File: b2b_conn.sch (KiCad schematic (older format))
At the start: 3 parts

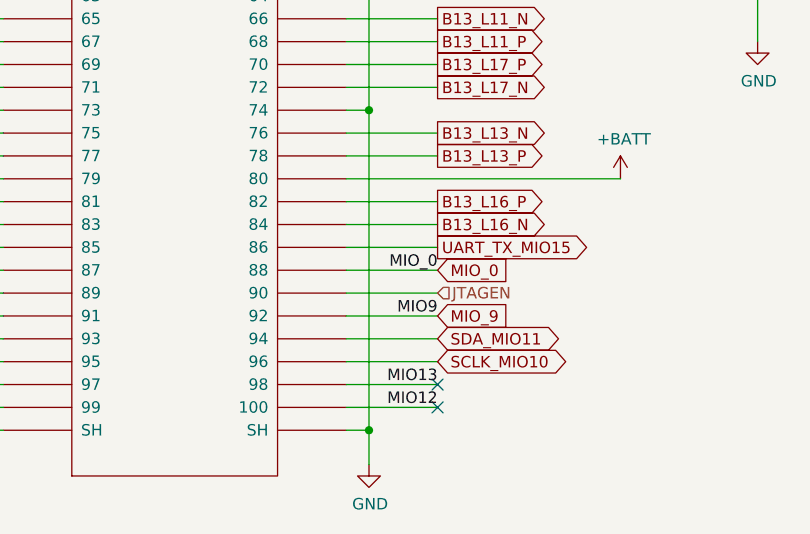
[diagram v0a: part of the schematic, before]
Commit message: b2b_conn.sch: removed redundant local labels (globals already present)
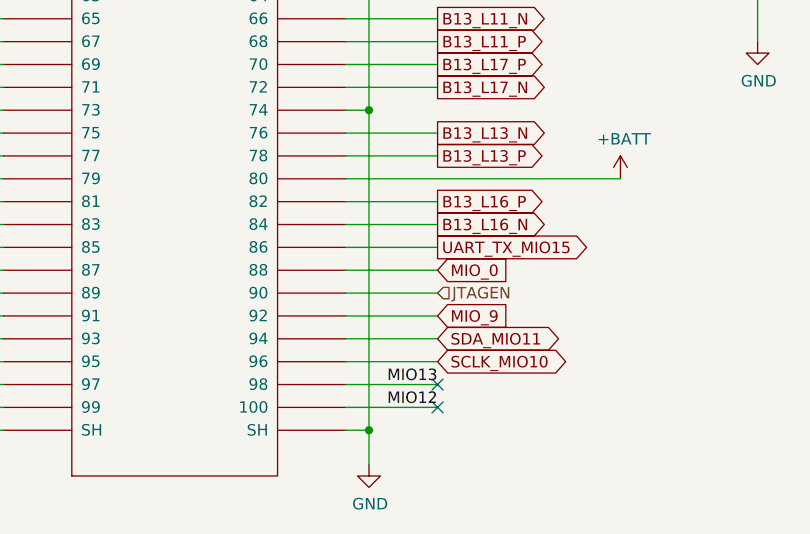
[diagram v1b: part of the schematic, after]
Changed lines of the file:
@@
 	3200 5300 3600 5300
-Wire Wire Line
-	3200 5500 3600 5500
 Wire Wire Line
 	3600 5700 3200 5700
@@
 Text GLabel 3600 2700 2    50   Output ~ 0
 B13_L3_P
-Text Label 3600 5500 2    50   ~ 0
-MIO_0
-Text Label 3600 5700 2    50   ~ 0
-MIO9
 NoConn ~ 1300 6000
 NoConn ~ 1300 6100
@@
 NoConn ~ 3600 6000
 NoConn ~ 3600 6100
+Wire Wire Line
+	3200 5500 3600 5500
 $EndSCHEMATC

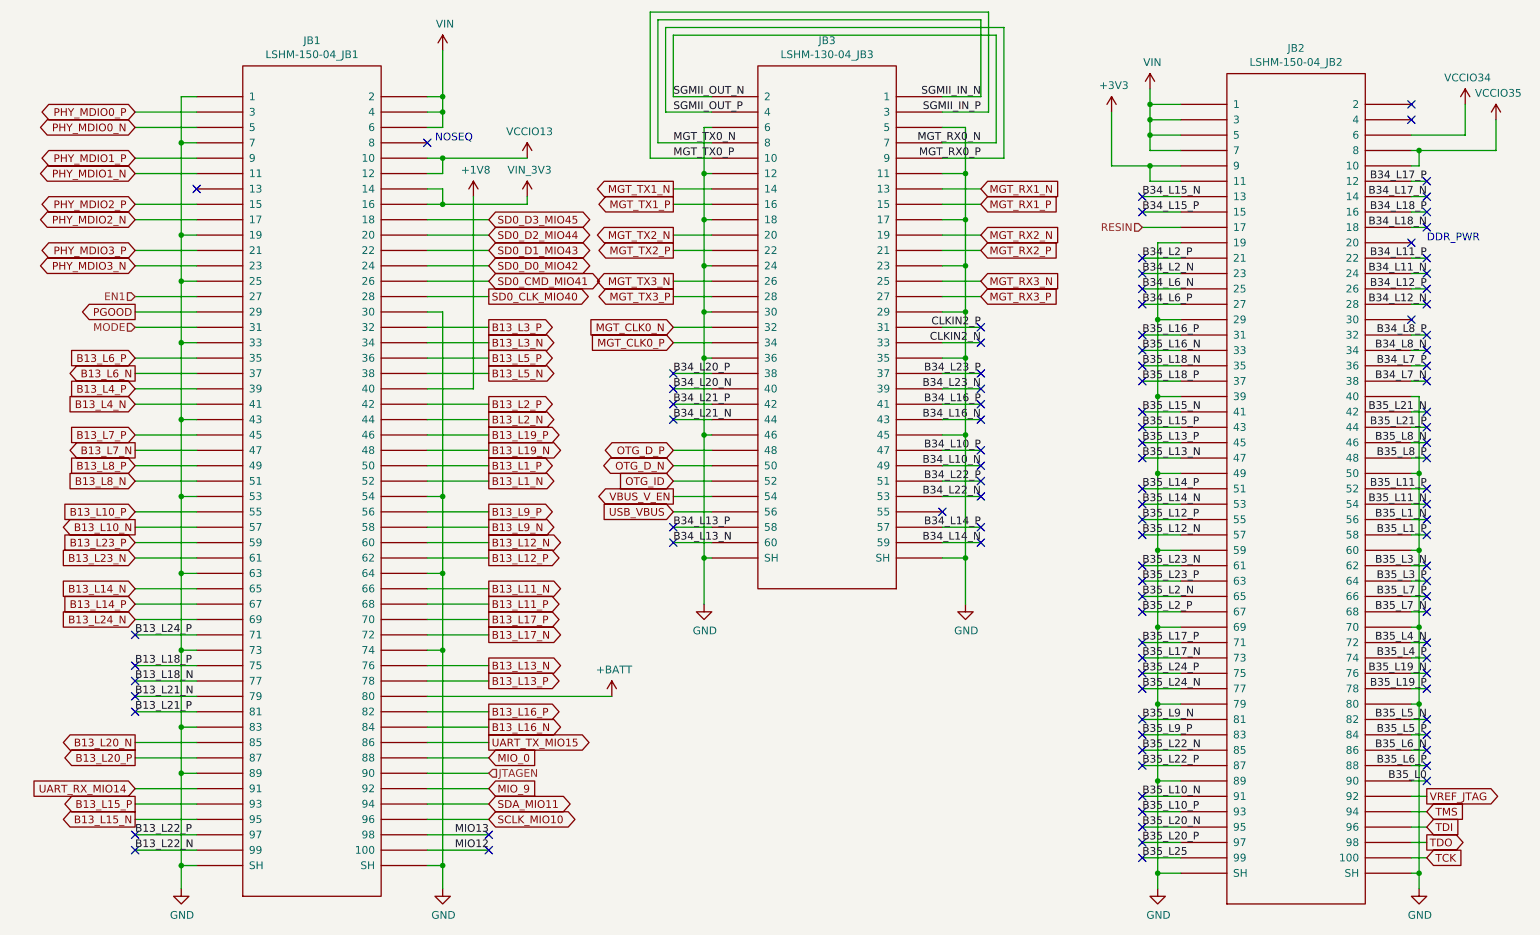
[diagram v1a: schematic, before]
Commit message: converted local- to global labels for B34/B34 B2B pins
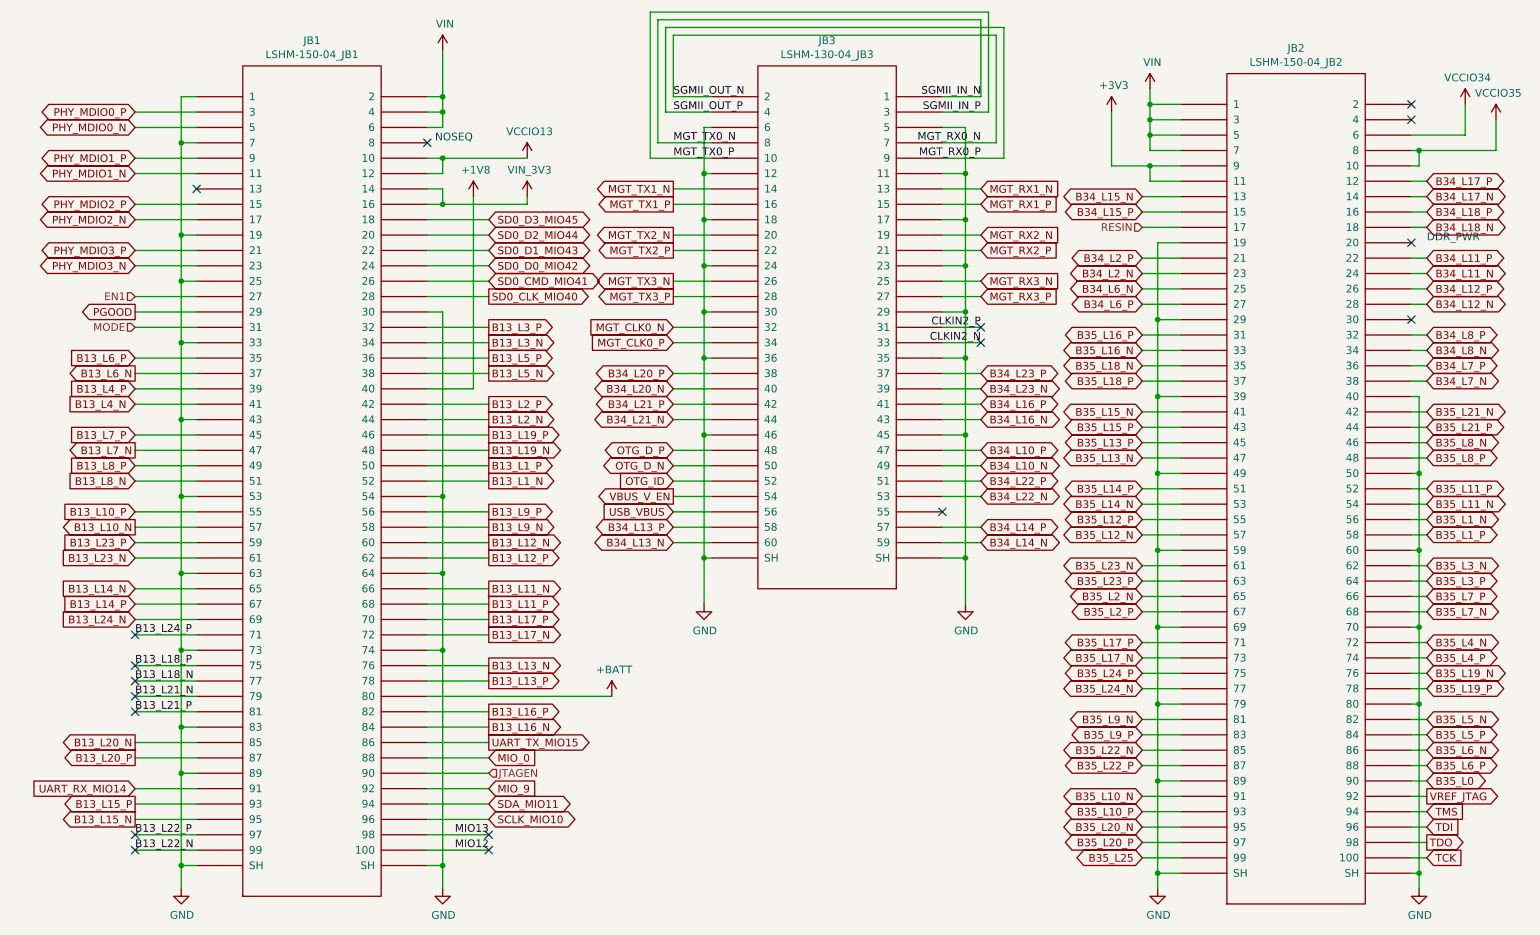
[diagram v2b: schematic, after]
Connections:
- no-connect marks 102 -> 18

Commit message: cont. work; all connections done now
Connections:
- no-connect marks 18 -> 14
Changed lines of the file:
@@
 Wire Wire Line
 	1700 4700 1300 4700
-Text Label 1300 4900 0    50   ~ 0
-B13_L18_P
-Text Label 1300 5000 0    50   ~ 0
-B13_L18_N
 Wire Wire Line
 	1700 4900 1300 4900
 Wire Wire Line
 	1700 5000 1300 5000
-Text Label 1300 5100 0    50   ~ 0
-B13_L21_N
-Text Label 1300 5200 0    50   ~ 0
-B13_L21_P
 Wire Wire Line
 	1700 5100 1300 5100
@@
 B13_L24_N
 NoConn ~ 1300 4700
-NoConn ~ 1300 4900
-NoConn ~ 1300 5000
-NoConn ~ 1300 5100
-NoConn ~ 1300 5200
 $Comp
 L te0715:LSHM-130-04_JB3 JB3
@@
 Wire Wire Line
 	6800 3100 6550 3100
+Text GLabel 1300 5200 0    50   Output ~ 0
+B13_L21_P
+Text GLabel 1300 5100 0    50   Output ~ 0
+B13_L21_N
+Text GLabel 1300 5000 0    50   Output ~ 0
+B13_L18_N
+Text GLabel 1300 4900 0    50   Output ~ 0
+B13_L18_P
 $EndSCHEMATC
